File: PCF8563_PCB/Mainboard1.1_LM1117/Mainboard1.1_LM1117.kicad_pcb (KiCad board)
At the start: 2 copper layers, 30 parts, among them J1 CONN_01X03, J2 CONN_01X15, J3 CONN_01X15, J4 SD_Card, J5 CONN_01X03, J6 CONN_01X02, J7 CONN_01X02, U1 LM1117-3.3, U2 PCF8563, Y1 Crystal

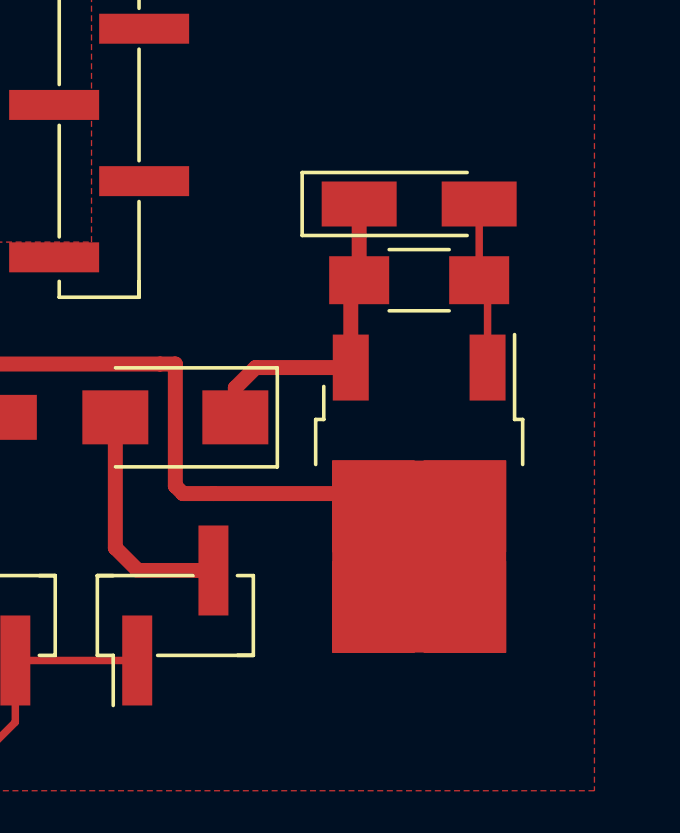
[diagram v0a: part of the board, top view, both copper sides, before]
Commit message: SettingsGenerator update
Added validating addresses in SettingsGenerator
Modified LM1117 board (SOT instead of DPAK voltage stabiliser)
Something I forgot
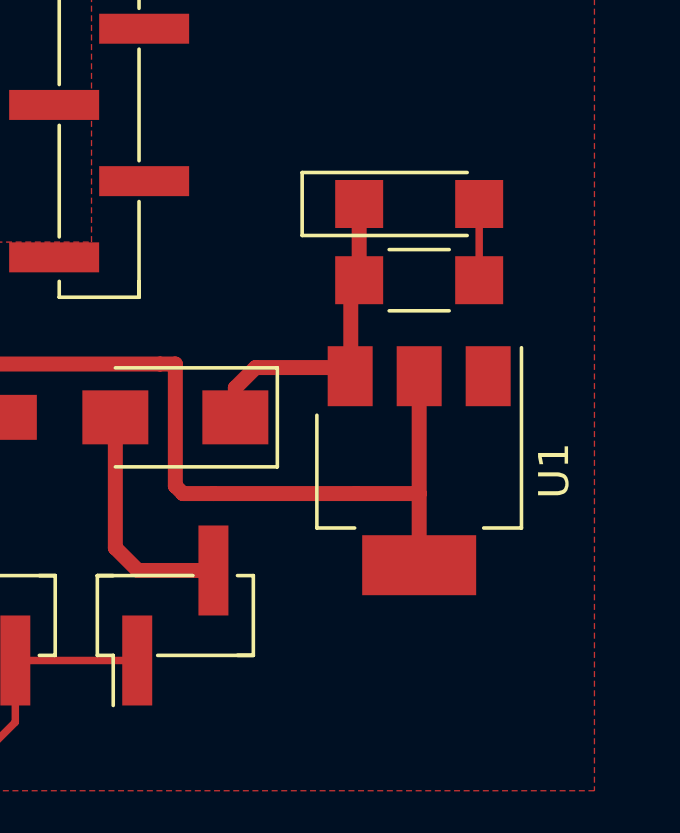
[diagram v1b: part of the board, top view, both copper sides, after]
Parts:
- U1: footprint TO_SOT_Packages_SMD:TO-252-2 -> TO_SOT_Packages_SMD:SOT-223-3Lead_TabPin2
- moved U1 0.76 mm to (170.7, 129.0)
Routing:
- net 3V3: track 150.3 -> 155.7 mm
- net GND: track 102.3 -> 99.7 mm
